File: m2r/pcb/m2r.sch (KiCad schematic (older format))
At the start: 0 parts

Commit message: place most major parts for m2r
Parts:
- added C?: CP1, symbol CP1
- added C?: C, symbol C
- added IC?: STM32F103C, symbol STM32F103C
- added IC?: APU1205-HF-3, symbol APU1205-HF-3
- added IC?: SP100-2T, symbol SP100-2T
- added IC?: ADL5324, symbol ADL5324
- added IC?: NTX2B, symbol NTX2B
- added IC? (x2): ADuM1201, symbol ADuM1201
- added IC?: MCP1802, symbol MCP1802
- added P?: SWD, symbol SWD
- added P?: CONN_2, symbol CONN_2
- added P?: RockBLOCK, symbol RockBLOCK
- added R?: R, symbol R
- added X?: CRYSTAL, symbol CRYSTAL
- added X?: BAT BOX, symbol PART
- added X?: ARM SW, symbol PART
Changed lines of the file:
@@
 LIBS:contrib
 LIBS:valves
+LIBS:part
+LIBS:sp100-2t
+LIBS:stm32f103c
+LIBS:swd
+LIBS:apu1205-hf-3
+LIBS:adl5324
+LIBS:ntx2b
+LIBS:rockblock
+LIBS:adum1201
+LIBS:mcp1802
+LIBS:m2r-cache
 EELAYER 24 0
 EELAYER END
@@
 Comment4 ""
 $EndDescr
+$Comp
+L STM32F103C IC?
+U 1 1 5378F592
+P 2550 5550
+F 0 "IC?" H 2900 7200 60  0000 C CNN
+F 1 "STM32F103C" H 2250 7200 60  0000 C CNN
+F 2 "" H 2650 5750 60  0000 C CNN
+F 3 "" H 2650 5750 60  0000 C CNN
+	1    2550 5550
+	1    0    0    -1
+$EndComp
+$Comp
+L CP1 C?
+U 1 1 5378F67E
+P 800 3950
+F 0 "C?" H 850 4050 50  0000 L CNN
+F 1 "CP1" H 850 3850 50  0000 L CNN
+F 2 "" H 800 3950 60  0000 C CNN
+F 3 "" H 800 3950 60  0000 C CNN
+	1    800  3950
+	1    0    0    -1
+$EndComp
+$Comp
+L C C?
+U 1 1 5378F77D
+P 1200 3950
+F 0 "C?" H 1200 4050 40  0000 L CNN
+F 1 "C" H 1206 3865 40  0000 L CNN
+F 2 "" H 1238 3800 30  0000 C CNN
+F 3 "" H 1200 3950 60  0000 C CNN
+	1    1200 3950
+	1    0    0    -1
+$EndComp
+$Comp
+L CRYSTAL X?
+U 1 1 5378F7D3
+P 1250 5400
+F 0 "X?" H 1250 5550 60  0000 C CNN
+F 1 "CRYSTAL" H 1250 5250 60  0000 C CNN
+F 2 "" H 1250 5400 60  0000 C CNN
+F 3 "" H 1250 5400 60  0000 C CNN
+	1    1250 5400
+	0    1    1    0
+$EndComp
+$Comp
+L R R?
+U 1 1 5378F8A6
+P 1600 5950
+F 0 "R?" V 1680 5950 40  0000 C CNN
+F 1 "R" V 1607 5951 40  0000 C CNN
+F 2 "" V 1530 5950 30  0000 C CNN
+F 3 "" H 1600 5950 30  0000 C CNN
+	1    1600 5950
+	1    0    0    -1
+$EndComp
+$Comp
+L SWD P?
+U 1 1 5378F982
+P 2000 3150
+F 0 "P?" H 2250 3450 60  0000 C CNN
+F 1 "SWD" H 1700 3450 60  0000 C CNN
+F 2 "" H 2350 2950 60  0000 C CNN
+F 3 "" H 2350 2950 60  0000 C CNN
+	1    2000 3150
+	1    0    0    -1
+$EndComp
+$Comp
+L APU1205-HF-3 IC?
+U 1 1 5378FAFF
+P 1350 1000
+F 0 "IC?" H 1400 800 60  0000 C CNN
+F 1 "APU1205-HF-3" H 1650 1200 60  0000 C CNN
+F 2 "" H 1350 1000 60  0000 C CNN
+F 3 "" H 1350 1000 60  0000 C CNN
+	1    1350 1000
+	1    0    0    -1
+$EndComp
+$Comp
+L PART X?
+U 1 1 5378FBAF
+P 800 1700
+F 0 "X?" H 850 1700 60  0000 C CNN
+F 1 "BAT BOX" H 950 1800 60  0000 C CNN
+F 2 "" H 800 1700 60  0000 C CNN
+F 3 "" H 800 1700 60  0000 C CNN
+	1    800  1700
+	1    0    0    -1
+$EndComp
+$Comp
+L PART X?
+U 1 1 5378FC77
+P 1450 1700
+F 0 "X?" H 1500 1700 60  0000 C CNN
+F 1 "ARM SW" H 1600 1800 60  0000 C CNN
+F 2 "" H 1450 1700 60  0000 C CNN
+F 3 "" H 1450 1700 60  0000 C CNN
+	1    1450 1700
+	1    0    0    -1
+$EndComp
+$Comp
+L CONN_2 P?
+U 1 1 5378FD2B
+P 700 1000
+F 0 "P?" V 650 1000 40  0000 C CNN
+F 1 "CONN_2" V 750 1000 40  0000 C CNN
+F 2 "" H 700 1000 60  0000 C CNN
+F 3 "" H 700 1000 60  0000 C CNN
+	1    700  1000
+	-1   0    0    1
+$EndComp
+$Comp
+L SP100-2T IC?
+U 1 1 5378FDA0
+P 3800 1600
+F 0 "IC?" H 4450 2400 60  0000 C CNN
+F 1 "SP100-2T" H 4100 2400 60  0000 C CNN
+F 2 "" H 3800 1600 60  0000 C CNN
+F 3 "" H 3800 1600 60  0000 C CNN
+	1    3800 1600
+	1    0    0    -1
+$EndComp
+$Comp
+L ADL5324 IC?
+U 1 1 53792B5C
+P 6100 3250
+F 0 "IC?" H 6050 3450 60  0000 C CNN
+F 1 "ADL5324" H 6150 3000 60  0000 C CNN
+F 2 "" H 6350 3100 60  0000 C CNN
+F 3 "" H 6350 3100 60  0000 C CNN
+	1    6100 3250
+	1    0    0    -1
+$EndComp
+$Comp
+L NTX2B IC?
+U 1 1 53793756
+P 5300 3300
+F 0 "IC?" H 5100 3550 60  0000 C CNN
+F 1 "NTX2B" H 5150 3050 60  0000 C CNN
+F 2 "" H 5300 3200 60  0000 C CNN
+F 3 "" H 5300 3200 60  0000 C CNN
+	1    5300 3300
+	1    0    0    -1
+$EndComp
+$Comp
+L RockBLOCK P?
+U 1 1 53793A78
+P 7550 2700
+F 0 "P?" H 7700 3200 60  0000 C CNN
+F 1 "RockBLOCK" H 7800 2100 60  0000 C CNN
+F 2 "" H 7550 2800 60  0000 C CNN
+F 3 "" H 7550 2800 60  0000 C CNN
+	1    7550 2700
+	1    0    0    -1
+$EndComp
+$Comp
+L ADuM1201 IC?
+U 1 1 53793B8D
+P 6950 2600
+F 0 "IC?" H 6800 2850 60  0000 C CNN
+F 1 "ADuM1201" H 6950 2350 60  0000 C CNN
+F 2 "" H 6950 2600 60  0000 C CNN
+F 3 "" H 6950 2600 60  0000 C CNN
+	1    6950 2600
+	1    0    0    -1
+$EndComp
+$Comp
+L ADuM1201 IC?
+U 1 1 53793C00
+P 8250 1000
+F 0 "IC?" H 8100 1250 60  0000 C CNN
+F 1 "ADuM1201" H 8250 750 60  0000 C CNN
+F 2 "" H 8250 1000 60  0000 C CNN
+F 3 "" H 8250 1000 60  0000 C CNN
+	1    8250 1000
+	1    0    0    -1
+$EndComp
+$Comp
+L MCP1802 IC?
+U 1 1 53796021
+P 2650 1050
+F 0 "IC?" H 2500 1300 60  0000 C CNN
+F 1 "MCP1802" H 2600 900 60  0000 C CNN
+F 2 "" H 2650 1050 60  0000 C CNN
+F 3 "" H 2650 1050 60  0000 C CNN
+F 4 "1578372" H 2650 1050 60  0001 C CNN "Farnell"
+	1    2650 1050
+	1    0    0    -1
+$EndComp
 $EndSCHEMATC

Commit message: add first go at m2r schematic
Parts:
- removed C?: CP1, symbol CP1
- removed C?: C, symbol C
- removed IC?: MCP1802, symbol MCP1802
- removed R?: R, symbol R
- added ANT1: JDGA_QUAD_V, symbol JDGA_QUAD_V
- added C1, C10, C13, C17, C2, C20, C24, C25, C26, C27, C29, C3, C30, C31, C34, C4, C5: 100n, 0603, symbol C
- added C11: 1n, 0603, symbol C
- added C12, C32, C6, C7, C8, C9: 2µ2, 0603, symbol CP1
- added C14: 100p, 0402, symbol C
- added C15: 10n, 0603, symbol C
- added C16: 10µ, 1206, symbol CP1
- added C18: 10p, 0402, symbol C
- added C19, C21: 20p, 0402, symbol C
- added C22: 6.2p, 0402, symbol C
- added C23: 10µ, 0603, symbol CP1
- added C28: 1µ, 0603, symbol CP1
- added C33: 4µ7, 0603, symbol CP1
- added C35, C36: 15p, 0603, symbol C
- added GS1, GS2: GS3, GS3, symbol GS3
- added IC1: ADP3338, symbol ADP3338
- added IC10: ALM-2712, symbol ALM-2712
- added IC12: TPS76327, symbol TPS76327
- added IC8: LTC2602, symbol LTC2602
- added IC9: MAX-7Q, symbol MAX-7Q
- added L1: 120n, 0603, symbol INDUCTOR_SMALL
- added L2: 1n6, 0603, symbol INDUCTOR_SMALL
- added L3: 5n6, 0402, symbol INDUCTOR_SMALL
- added P2: CONN_4, symbol CONN_4
- added P5: SMA, symbol SMA
- added R1, R2: 10k, 0603, symbol R
- added R3: 1k, 0603, symbol R
- added R4: 2, 0402, symbol R
- added R5: 6k8, 0603, symbol R
- added R6: 100, 0603, symbol R
- IC2: renamed from IC?; Farnell (none) -> 2319654
- IC3, IC4: renamed from IC?; Farnell (none) -> 1078200
- IC5: renamed from IC?; Farnell (none) -> 1845351
- IC6: renamed from IC?; Farnell (none) -> 2099794
- P1: renamed from P?; Farnell (none) -> 1462926
- P4: renamed from P?; Farnell (none) -> 1667759
- X1: renamed from X?; Farnell (none) -> BT01732
- X2: renamed from X?; Farnell (none) -> 149288
- gave numbers to parts that had none: 4
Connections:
- net labels added: +3.3V, +5V, +BATT, BARO_CS, BARO_MISO, BARO_MOSI, BARO_SCK, BAT_MON, DAC_CS, DAC_SCK, DAC_SDI, GND, GPS_RX, GPS_TX, NTX2B_EN, RB_RX, RB_TX, SER_IN, SER_OUT, SWCLK, SWDIO, SWO, nRST
- wire segments 0 -> 296
- no-connect marks 0 -> 31
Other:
- note added: "BAROMETER"
- note added: "BATTERY MONITORING"
- note added: "COMPONENT PLACEMENT CRITICAL\nREFER TO ADL5324 DATASHEET FIGURE 41"
- note added: "GPS"
- note added: "MICROCONTROLLER"
- note added: "POWER SUPPLY"
- note added: "RADIO DOWNLINK"
- note added: "RockBLOCK SATELLITE MODEM"
- note added: "SERIAL IN/OUT"
- note added: "SERIAL WIRE DEBUG"
- moved on the sheet: IC11, IC2, IC3, IC4, IC5, IC6, IC7, P1, P3, P4, X1, X2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

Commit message: spec crystal part
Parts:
- X3: value CRYSTAL -> 8M; footprint (none) -> HC49/S; Farnell (none) -> 2063945
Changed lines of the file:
@@
 P 1500 5850
 F 0 "X3" H 1500 6000 60  0000 C CNN
-F 1 "CRYSTAL" H 1500 5700 60  0000 C CNN
-F 2 "" H 1500 5850 60  0000 C CNN
+F 1 "8M" H 1500 5700 60  0000 C CNN
+F 2 "HC49/S" H 1500 5850 60  0001 C CNN
 F 3 "" H 1500 5850 60  0000 C CNN
+F 4 "2063945" H 1500 5850 60  0001 C CNN "Farnell"
 	1    1500 5850
 	0    1    1    0

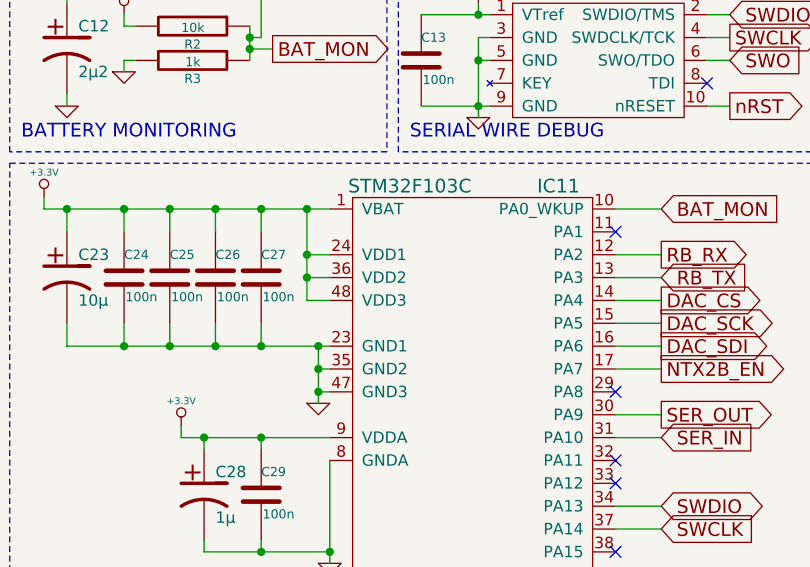
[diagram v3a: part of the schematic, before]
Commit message: swap STM32F103 for STM32F303
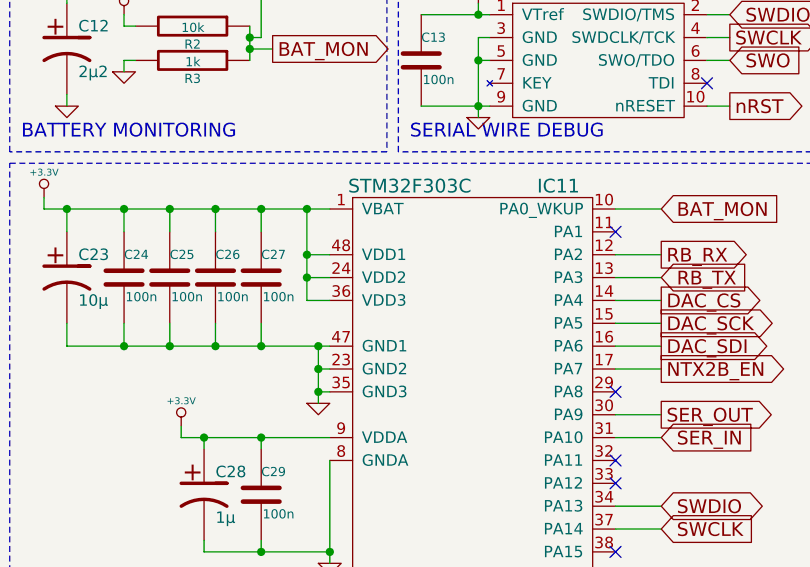
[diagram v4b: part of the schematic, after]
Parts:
- removed IC11: STM32F103C, symbol STM32F103C
- added IC11: STM32F303C, symbol STM32F303C
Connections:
- net +3.3V: now also IC11.1 (VBAT), IC11.24 (VDD2), IC11.36 (VDD3), IC11.48 (VDD1), IC11.9 (VDDA)
- net BARO_CS: now also IC11.25 (PB12)
- net BARO_MISO: now also IC11.27 (PB14)
- net BARO_MOSI: now also IC11.28 (PB15)
- net BARO_SCK: now also IC11.26 (PB13)
- net BAT_MON: now also IC11.10 (PA0_WKUP)
- net DAC_CS: now also IC11.14 (PA4)
- net DAC_SCK: now also IC11.15 (PA5)
- net DAC_SDI: now also IC11.16 (PA6)
- net GND: now also IC11.23 (GND2), IC11.35 (GND3), IC11.44 (BOOT0), IC11.47 (GND1), IC11.8 (GNDA)
- net GPS_RX: now also IC11.21 (PB10)
- net GPS_TX: now also IC11.22 (PB11)
- net NTX2B_EN: now also IC11.17 (PA7)
- net RB_RX: now also IC11.12 (PA2)
- net RB_TX: now also IC11.13 (PA3)
- net SER_IN: now also IC11.31 (PA10)
- net SER_OUT: now also IC11.30 (PA9)
- net SWCLK: now also IC11.37 (PA14)
- net SWDIO: now also IC11.34 (PA13)
- net SWO: now also IC11.39 (PB3)
- net nRST: now also IC11.7 (NRST)
- net at C35.1, X3.1: now also IC11.5 (PD0_OSCIN)
- net at R6.2: now also IC11.6 (PD1_OSCOUT)

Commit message: finish up m2r schematic
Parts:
- removed C20: 100n, 0603, symbol C
- removed IC8: LTC2602, symbol LTC2602
- added D1, D2: RED, 0603, symbol LED
- added D3, D4, D5, D6: YELLOW, 0603, symbol LED
- added P6: CONN_2, symbol CONN_2
- added R10, R11, R12, R13, R6, R8, R9: 100, 0603, symbol R
- added R5: 50, 0603, symbol R
- added TP1, TP10, TP11, TP12, TP13, TP14, TP15, TP16, TP17, TP18, TP19, TP2, TP20, TP21, TP22, TP3, TP4, TP5, TP6, TP7, TP8, TP9: TESTPAD, symbol TESTPAD
- added X3: RG LED, symbol PART
- renumbered C21 to C20, C22 to C21, C23 to C22, C24 to C23, C25 to C24, C26 to C25, C27 to C26, C28 to C27, C29 to C28, C30 to C29, C31 to C30, C32 to C31, C33 to C32, C34 to C33, C35 to C34, C36 to C35, IC11 to IC10, IC12 to IC11, IC9 to IC8, IC10 to IC9, R6 to R14, R5 to R7, X3 to X4
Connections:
- net DAC_CS is gone; now on net NTX2B_TXD: IC10.14 (PA4)
- net +3.3V: now also R8.2, TP2.1 (TP)
- net +5V: now also R9.2, TP3.1 (TP)
- net +BATT: now also TP1.1 (TP)
- net BARO_CS: now also TP19.1 (TP)
- net BARO_MISO: now also TP21.1 (TP)
- net BARO_MOSI: now also TP22.1 (TP)
- net BARO_SCK: now also TP20.1 (TP)
- net BAT_MON: now also TP9.1 (TP)
- net GND: now also D1.2 (K), D2.2 (K), D3.2 (K), D4.2 (K), D5.2 (K), D6.2 (K), TP5.1 (TP)
- net GPS_RX: now also TP17.1 (TP)
- net GPS_TX: now also TP18.1 (TP)
- net NTX2B_EN: now also TP13.1 (TP)
- net RB_RX: now also TP10.1 (TP)
- net RB_TX: now also TP11.1 (TP)
- net SER_IN: now also TP15.1 (TP)
- net SER_OUT: now also TP14.1 (TP)
- net NTX2B_TXD: now reaches IC7.7 (TXD)
- net NTX2B_TXD: now also TP12.1 (TP)
- net at IC4.7 (IN_A), P3.3 (TXO): now also TP4.1 (TP)
- net at IC4.6 (OUT_B), P3.4 (RXI): now also TP7.1 (TP)
- net at IC3.6 (OUT_B), P2.3 (P3): now also TP8.1 (TP)
- net at IC3.7 (IN_A), P2.2 (P2): now also TP6.1 (TP)
- net LED_1: now reaches IC10.40 (PB4)
- net LED_1: now also R10.2
- net LED_2: now reaches IC10.41 (PB5)
- net LED_2: now also R12.2
- net LED_3: now reaches IC10.42 (PB6)
- net LED_3: now also R11.2
- net LED_4: now reaches IC10.43 (PB7)
- net LED_4: now also R13.2
- net LED_A: now reaches IC10.45 (PB8)
- net LED_A: now also R5.2
- net LED_C: now reaches IC10.46 (PB9)
- net LED_C: now also P6.2 (PM)
- net at C30.1, C32.1, IC11.5 (OUT)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: now also TP16.1 (TP)
- net DAC_SCK: no longer names the net of IC10.15 (PA5)
- net DAC_SDI: no longer names the net of IC10.16 (PA6)
- new net: P6.1 (P1), R5.1
- new net: D1.1 (A), R8.1
- new net: D3.1 (A), R10.1
- new net: R6.2, R9.1
- new net: D2.1 (A), R6.1
- new net: D4.1 (A), R11.1
- new net: D6.1 (A), R13.1
- new net: D5.1 (A), R12.1
- no-connect marks 31 -> 26
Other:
- note added: "EXTERNAL STATUS LED"
- moved on the sheet: C14, C15, C16, C17, C18, C19, C20, C21, GS1, GS2, IC6, IC7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

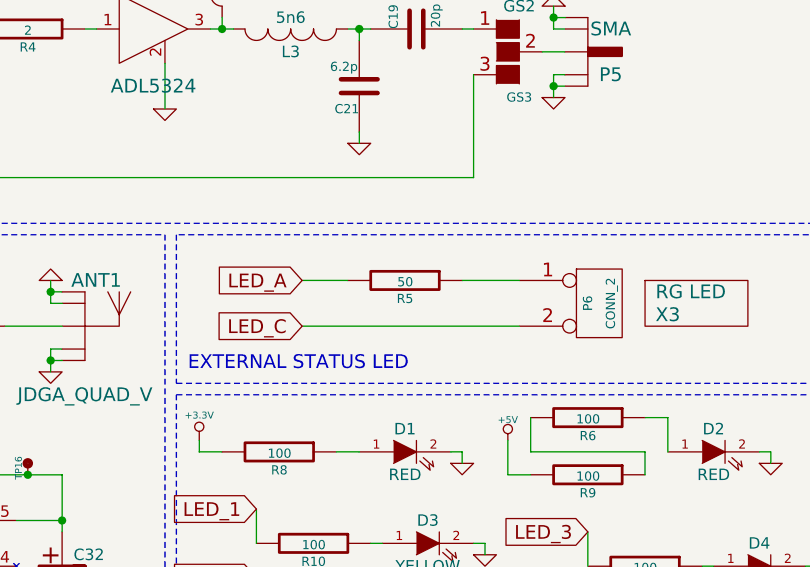
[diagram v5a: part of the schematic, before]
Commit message: use two 100R to make up 50R because lol
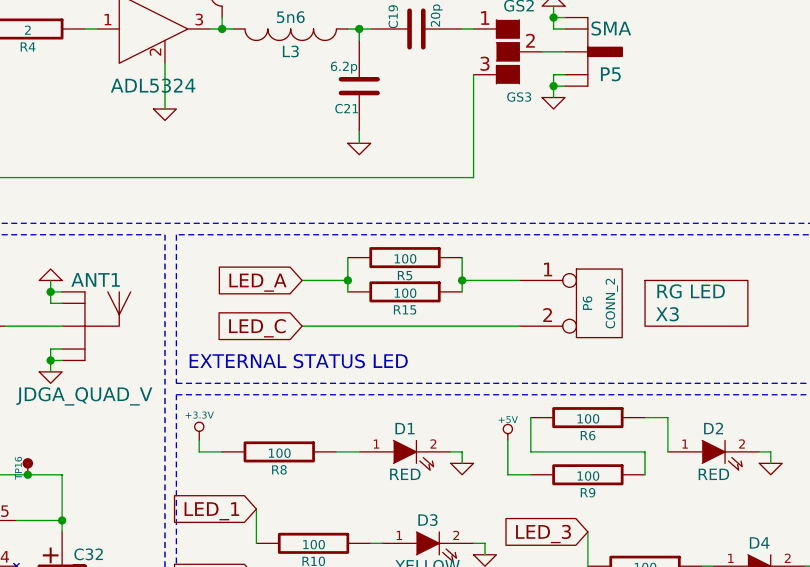
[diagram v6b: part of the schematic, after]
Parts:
- added R15: 100, 0603, symbol R
- R5: value 50 -> 100; Farnell 2331983 -> 2331989
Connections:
- net LED_A: now also R15.2
- net at P6.1 (P1), R5.1: now also R15.1
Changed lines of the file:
@@
 LED_C
-$Comp
-L R R5
-U 1 1 537FF90F
-P 9350 3800
-F 0 "R5" V 9430 3800 40  0000 C CNN
-F 1 "50" V 9357 3801 40  0000 C CNN
-F 2 "0603" V 9280 3800 30  0001 C CNN
-F 3 "" H 9350 3800 30  0000 C CNN
-F 4 "2331983" H 9350 3800 60  0001 C CNN "Farnell"
-	1    9350 3800
-	0    1    1    0
-$EndComp
 $Comp
 L CONN_2 P6
@@
 Wire Wire Line
 	3150 5400 3350 5400
+$Comp
+L R R15
+U 1 1 53825093
+P 9350 3850
+F 0 "R15" V 9430 3850 40  0000 C CNN
+F 1 "100" V 9357 3851 40  0000 C CNN
+F 2 "0603" V 9280 3850 30  0001 C CNN
+F 3 "" H 9350 3850 30  0000 C CNN
+F 4 "2331989" H 9350 3850 60  0001 C CNN "Farnell"
+	1    9350 3850
+	0    1    1    0
+$EndComp
+$Comp
+L R R5
+U 1 1 53825371
+P 9350 3700
+F 0 "R5" V 9430 3700 40  0000 C CNN
+F 1 "100" V 9357 3701 40  0000 C CNN
+F 2 "0603" V 9280 3700 30  0001 C CNN
+F 3 "" H 9350 3700 30  0000 C CNN
+F 4 "2331989" H 9350 3700 60  0001 C CNN "Farnell"
+	1    9350 3700
+	0    1    1    0
+$EndComp
+Wire Wire Line
+	9100 3700 9100 3850
+Connection ~ 9100 3800
+Wire Wire Line
+	9600 3700 9600 3850
+Connection ~ 9600 3800
 $EndSCHEMATC
